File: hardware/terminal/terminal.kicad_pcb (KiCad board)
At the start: 2 copper layers, 60 x 40 mm, 31 parts, among them IC1 ATMEGA8-P, J1 RJ45, P1 Prog, P10 CONN_4, P11 CONN_5X2, P12 CONN_4, P13 CONN_3X2, P14 CONN_5X2, P2 RC522, P3 LCD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

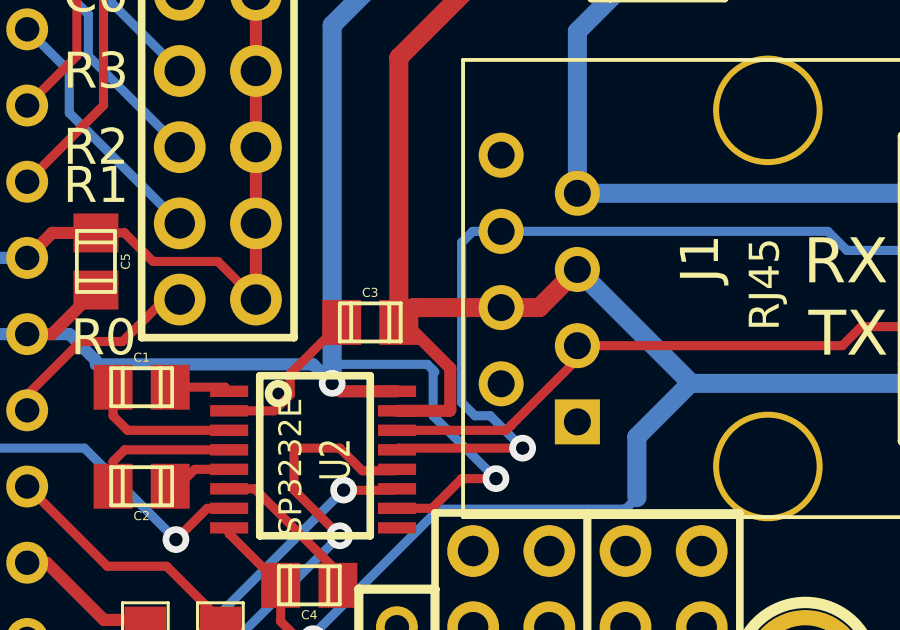
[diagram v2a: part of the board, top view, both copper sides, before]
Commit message: o Make DRC happy: it wanted an explicit track between two pads even  though they were already connected. Ah well.
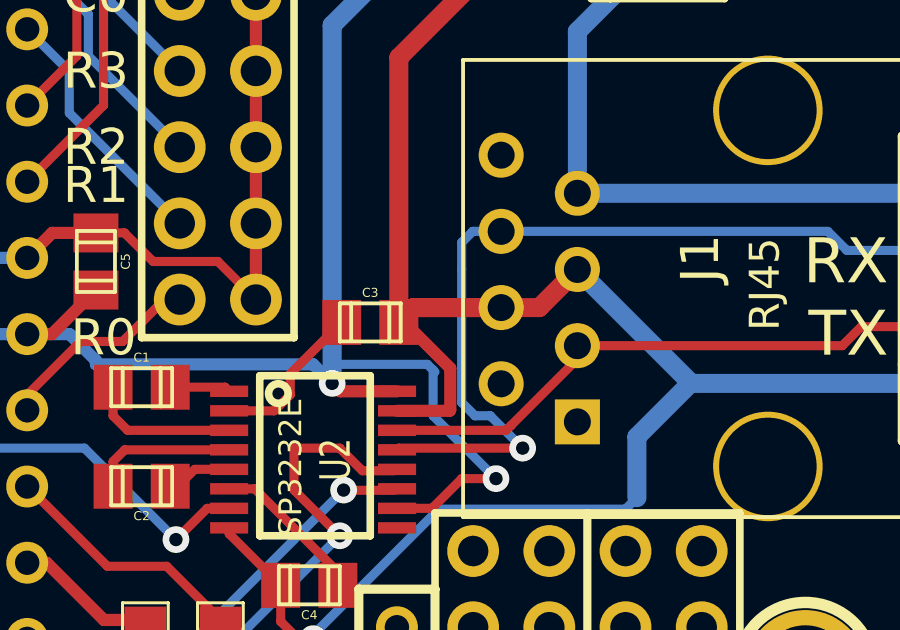
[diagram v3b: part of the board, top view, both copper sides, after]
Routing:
- net GND: track 196.4 -> 200.0 mm
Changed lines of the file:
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@@
     (thickness 1.6)
     (drawings 43)
-    (tracks 330)
+    (tracks 332)
     (zones 0)
     (modules 31)
@@
   (segment (start 152.64638 60.77712) (end 153.79192 60.77712) (width 0.3048) (layer F.Cu) (net 4))
   (segment (start 151.8285 61.595) (end 152.64638 60.77712) (width 0.3048) (layer F.Cu) (net 4))
+  (segment (start 162.86 55.385) (end 159.9435 55.385) (width 0.635) (layer F.Cu) (net 5))
+  (segment (start 159.9435 55.385) (end 159.4485 55.88) (width 0.635) (layer F.Cu) (net 5))
   (segment (start 169.1805 57.8955) (end 167.386 59.69) (width 0.635) (layer B.Cu) (net 5))
   (segment (start 167.386 59.69) (end 167.386 61.722) (width 0.635) (layer B.Cu) (net 5))
-  (segment (start 165.4 54.115) (end 169.1805 57.8955) (width 0.635) (layer B.Cu) (net 5) (status 400000))
+  (segment (start 165.4 54.115) (end 169.1805 57.8955) (width 0.635) (layer B.Cu) (net 5))
   (segment (start 169.1805 57.8955) (end 169.197 57.912) (width 0.635) (layer B.Cu) (net 5))
-  (segment (start 169.197 57.912) (end 176.852 57.912) (width 0.635) (layer B.Cu) (net 5) (status 800000))
-  (segment (start 176.852 57.912) (end 177.5 58.56) (width 0.635) (layer B.Cu) (net 5) (status C00000))
-  (segment (start 165.4 54.115) (end 164.13 55.385) (width 0.635) (layer F.Cu) (net 5) (status 400000))
-  (segment (start 164.13 55.385) (end 159.9435 55.385) (width 0.635) (layer F.Cu) (net 5) (status 800000))
-  (segment (start 159.9435 55.385) (end 159.4485 55.88) (width 0.635) (layer F.Cu) (net 5) (status C00000))
-  (segment (start 168.402 40.64) (end 165.862 40.64) (width 0.635) (layer F.Cu) (net 5) (status 400000))
-  (segment (start 159.4485 47.0535) (end 159.4485 55.88) (width 0.635) (layer F.Cu) (net 5) (status 800000))
+  (segment (start 169.197 57.912) (end 176.852 57.912) (width 0.635) (layer B.Cu) (net 5))
+  (segment (start 176.852 57.912) (end 177.5 58.56) (width 0.635) (layer B.Cu) (net 5))
+  (segment (start 165.4 54.115) (end 164.13 55.385) (width 0.635) (layer F.Cu) (net 5))
+  (segment (start 164.13 55.385) (end 159.9435 55.385) (width 0.635) (layer F.Cu) (net 5))
+  (segment (start 159.9435 55.385) (end 159.4485 55.88) (width 0.635) (layer F.Cu) (net 5))
+  (segment (start 168.402 40.64) (end 165.862 40.64) (width 0.635) (layer F.Cu) (net 5))
+  (segment (start 159.4485 47.0535) (end 159.4485 55.88) (width 0.635) (layer F.Cu) (net 5))
   (segment (start 165.862 40.64) (end 159.4485 47.0535) (width 0.635) (layer F.Cu) (net 5))
-  (segment (start 154.686 42.418) (end 156.464 40.64) (width 0.635) (layer F.Cu) (net 5) (status 400000))
-  (segment (start 156.464 40.64) (end 168.402 40.64) (width 0.635) (layer F.Cu) (net 5) (status 800000))
+  (segment (start 154.686 42.418) (end 156.464 40.64) (width 0.635) (layer F.Cu) (net 5))
+  (segment (start 156.464 40.64) (end 168.402 40.64) (width 0.635) (layer F.Cu) (net 5))
   (segment (start 124.841 65.0875) (end 124.968 65.2145) (width 0.3048) (layer F.Cu) (net 5))
   (segment (start 124.968 65.2145) (end 124.968 70.358) (width 0.3048) (layer F.Cu) (net 5))
@@
   (segment (start 151.638 55.118) (end 150.241 56.515) (width 0.3048) (layer F.Cu) (net 12))
   (segment (start 152.146 55.118) (end 151.638 55.118) (width 0.3048) (layer F.Cu) (net 12))
-  (segment (start 168.402 38.1) (end 165.1 38.1) (width 0.635) (layer B.Cu) (net 13) (status 400000))
+  (segment (start 168.402 38.1) (end 165.1 38.1) (width 0.635) (layer B.Cu) (net 13))
   (segment (start 164.338 38.862) (end 157.226 45.974) (width 0.635) (layer B.Cu) (net 13))
   (segment (start 157.226 45.974) (end 157.226 57.912) (width 0.635) (layer B.Cu) (net 13))
@@
   (segment (start 139.44 70.352) (end 139.44 71.51) (width 0.3048) (layer F.Cu) (net 32))
   (segment (start 130.81 60.706) (end 135.255 65.151) (width 0.3048) (layer F.Cu) (net 32))
-  (segment (start 177.5 50.94) (end 176.865 51.575) (width 0.635) (layer B.Cu) (net 35) (status 400000))
-  (segment (start 176.865 51.575) (end 165.4 51.575) (width 0.635) (layer B.Cu) (net 35) (status 800000))
-  (segment (start 168.402 43.18) (end 165.4 46.182) (width 0.635) (layer B.Cu) (net 35) (status 400000))
+  (segment (start 177.5 50.94) (end 176.865 51.575) (width 0.635) (layer B.Cu) (net 35))
+  (segment (start 176.865 51.575) (end 165.4 51.575) (width 0.635) (layer B.Cu) (net 35))
+  (segment (start 168.402 43.18) (end 165.4 46.182) (width 0.635) (layer B.Cu) (net 35))
   (segment (start 165.4 46.182) (end 165.4 51.575) (width 0.635) (layer B.Cu) (net 35))
   (segment (start 123.5075 71.755) (end 125.1585 73.406) (width 0.3048) (layer F.Cu) (net 41))

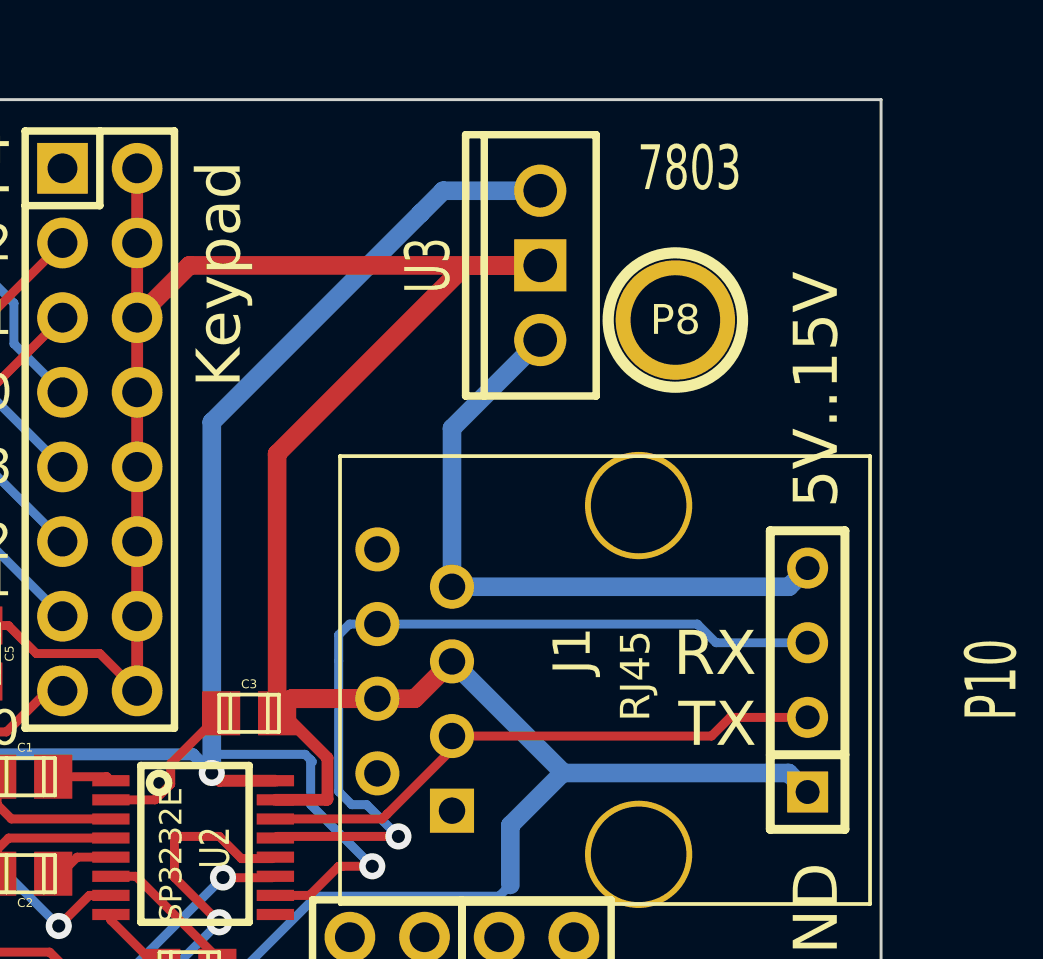
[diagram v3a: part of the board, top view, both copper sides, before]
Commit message: o Add option for input filter cap.
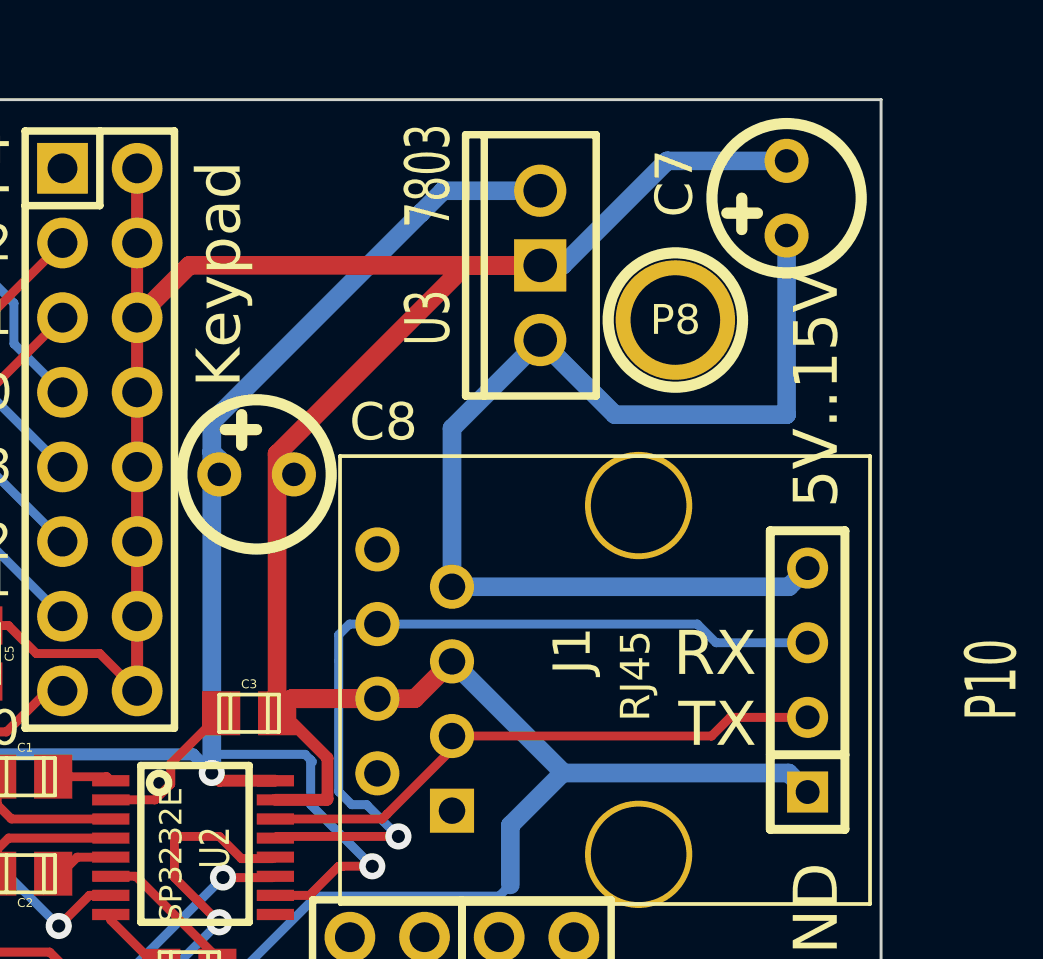
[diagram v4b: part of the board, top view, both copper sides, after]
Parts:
- added C7: CP, Capacitors_Elko_ThroughHole:Elko_vert_DM5_RM2-5, F.Cu at (176.8, 38.4)
- added C8: CP, Capacitors_Elko_ThroughHole:Elko_vert_DM5_RM2-5, F.Cu at (158.8, 47.8)
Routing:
- net +12V: track 22.0 -> 37.5 mm
- net GND: track 200.0 -> 210.8 mm
- net +3.3V: track 142.6 -> 143.5 mm

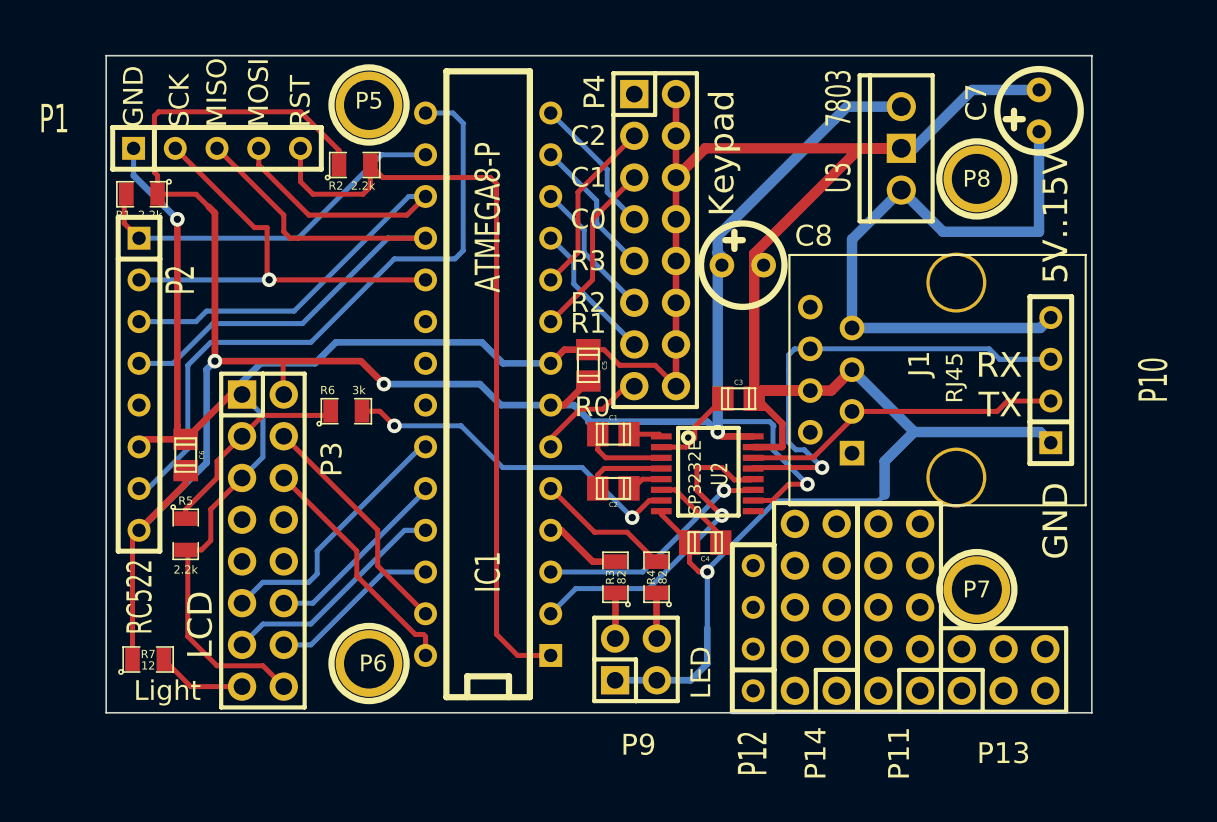
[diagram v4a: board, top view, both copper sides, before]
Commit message: o Ground flooding.
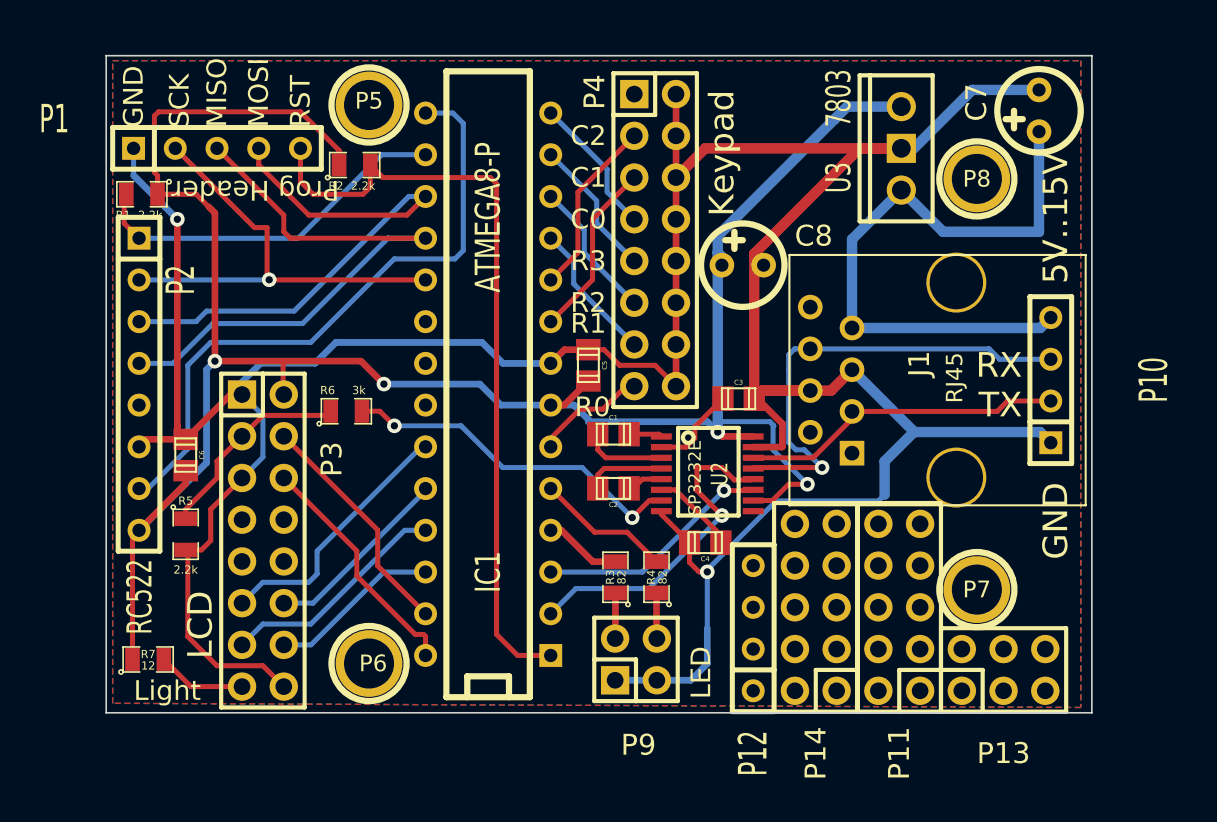
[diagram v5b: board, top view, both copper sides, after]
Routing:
- added copper zone on B.Cu, net GND
- added copper zone on F.Cu, net GND
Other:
- board text added: "Prog Header"

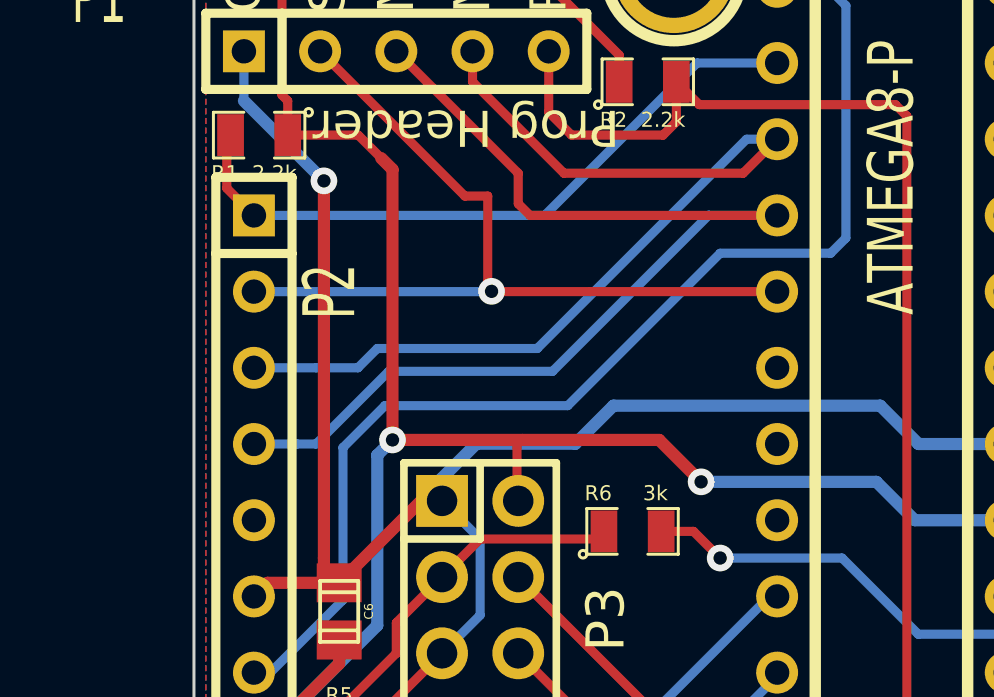
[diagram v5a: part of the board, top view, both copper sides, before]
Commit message: o Adding a logo is a freakin' nightmare in KiCAD. So just added   text attribution to Noisebridge and author.
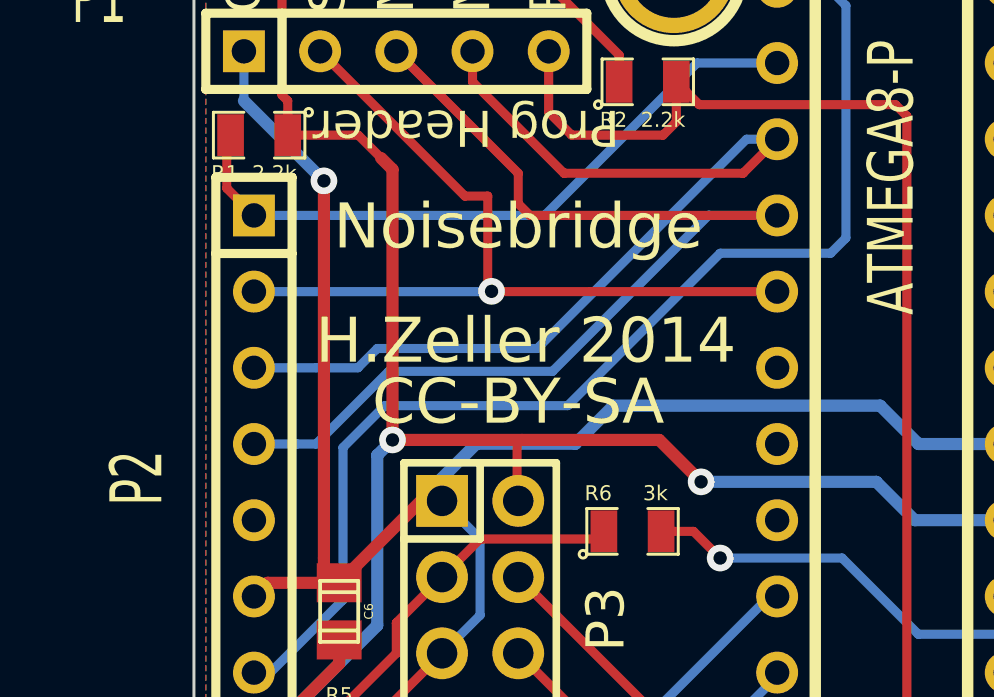
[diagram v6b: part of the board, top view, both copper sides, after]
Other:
- board text added: "CC-BY-SA"
- board text added: "H.Zeller 2014"
- board text added: "Noisebridge"
- board text added: "github.com/hzeller/rfid-access-control"
